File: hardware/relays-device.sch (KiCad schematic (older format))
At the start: 0 parts

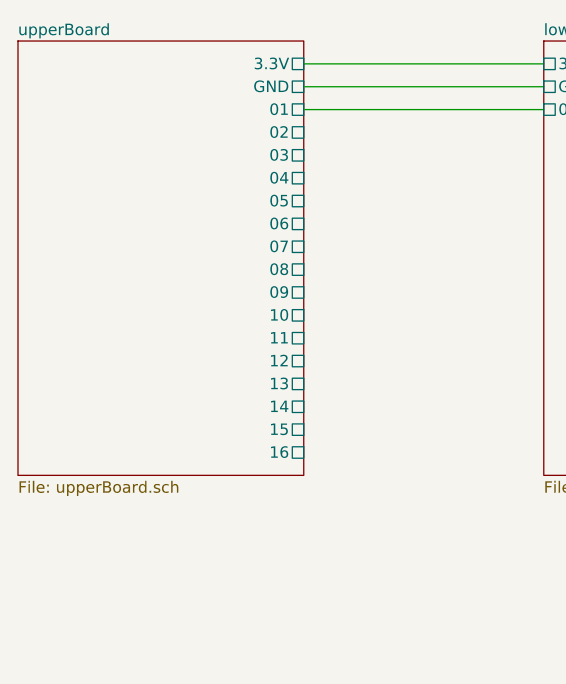
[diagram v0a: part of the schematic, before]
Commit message: replaced separated driver parts with driver chips and LED bars
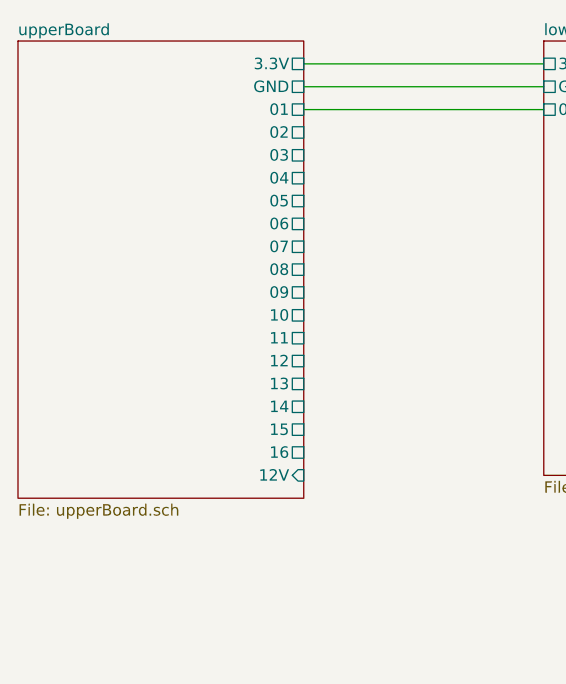
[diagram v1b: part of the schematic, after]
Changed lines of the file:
@@
 EESchema Schematic File Version 4
-LIBS:heating-control-cache
+LIBS:relays-device-cache
 EELAYER 30 0
 EELAYER END
 $Descr A4 11693 8268
 encoding utf-8
-Sheet 1 4
+Sheet 1 3
 Title ""
 Date ""
@@
 $EndDescr
 $Sheet
-S 1450 1450 1250 1900
+S 1450 1450 1250 2000
 U 5D9B8E7D
 F0 "upperBoard" 50
@@
 F18 "04" U R 2700 2050 50
 F19 "02" U R 2700 1850 50
+F20 "12V" I R 2700 3350 50
 $EndSheet
 $Sheet

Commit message: extracted relay to sub schematic to be able to multiply it
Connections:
- net labels removed: +12V, GND
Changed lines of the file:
@@
 $Descr A4 11693 8268
 encoding utf-8
-Sheet 1 3
+Sheet 1 5
 Title ""
 Date ""
@@
 F18 "04" U R 2700 2050 50
 F19 "02" U R 2700 1850 50
-F20 "12V" I R 2700 3350 50
+F20 "12V" U R 2700 3350 50
 $EndSheet
 $Sheet
-S 3750 1450 1250 1900
+S 3750 1450 1150 2000
 U 5D9FF064
 F0 "lowerBoard" 50
@@
 F3 "GND" U L 3750 1650 50
 F4 "01" U L 3750 1750 50
+F5 "12V" U L 3750 3350 50
+F6 "02" U L 3750 1850 50
 $EndSheet
 Wire Wire Line
@@
 Wire Wire Line
 	2700 1750 3750 1750
-$Comp
-L power:GND #PWR0102
-U 1 1 5DC08160
-P 3850 5200
-F 0 "#PWR0102" H 3850 4950 50  0001 C CNN
-F 1 "GND" H 3855 5027 50  0000 C CNN
-F 2 "" H 3850 5200 50  0001 C CNN
-F 3 "" H 3850 5200 50  0001 C CNN
-	1    3850 5200
-	1    0    0    -1
-$EndComp
-$Comp
-L power:PWR_FLAG #FLG0101
-U 1 1 5DC086BC
-P 3850 4900
-F 0 "#FLG0101" H 3850 4975 50  0001 C CNN
-F 1 "PWR_FLAG" H 3850 5073 50  0000 C CNN
-F 2 "" H 3850 4900 50  0001 C CNN
-F 3 "~" H 3850 4900 50  0001 C CNN
-	1    3850 4900
-	1    0    0    -1
-$EndComp
-$Comp
-L power:+12V #PWR0103
-U 1 1 5DC089A8
-P 3400 4900
-F 0 "#PWR0103" H 3400 4750 50  0001 C CNN
-F 1 "+12V" H 3415 5073 50  0000 C CNN
-F 2 "" H 3400 4900 50  0001 C CNN
-F 3 "" H 3400 4900 50  0001 C CNN
-	1    3400 4900
-	1    0    0    -1
-$EndComp
-$Comp
-L power:PWR_FLAG #FLG0102
-U 1 1 5DC08CFD
-P 3400 5200
-F 0 "#FLG0102" H 3400 5275 50  0001 C CNN
-F 1 "PWR_FLAG" H 3400 5373 50  0000 C CNN
-F 2 "" H 3400 5200 50  0001 C CNN
-F 3 "~" H 3400 5200 50  0001 C CNN
-	1    3400 5200
-	-1   0    0    1
-$EndComp
 Wire Wire Line
-	3850 5200 3850 4900
+	2700 3350 3750 3350
 Wire Wire Line
-	3400 5200 3400 4900
+	2700 1850 3750 1850
 $EndSCHEMATC

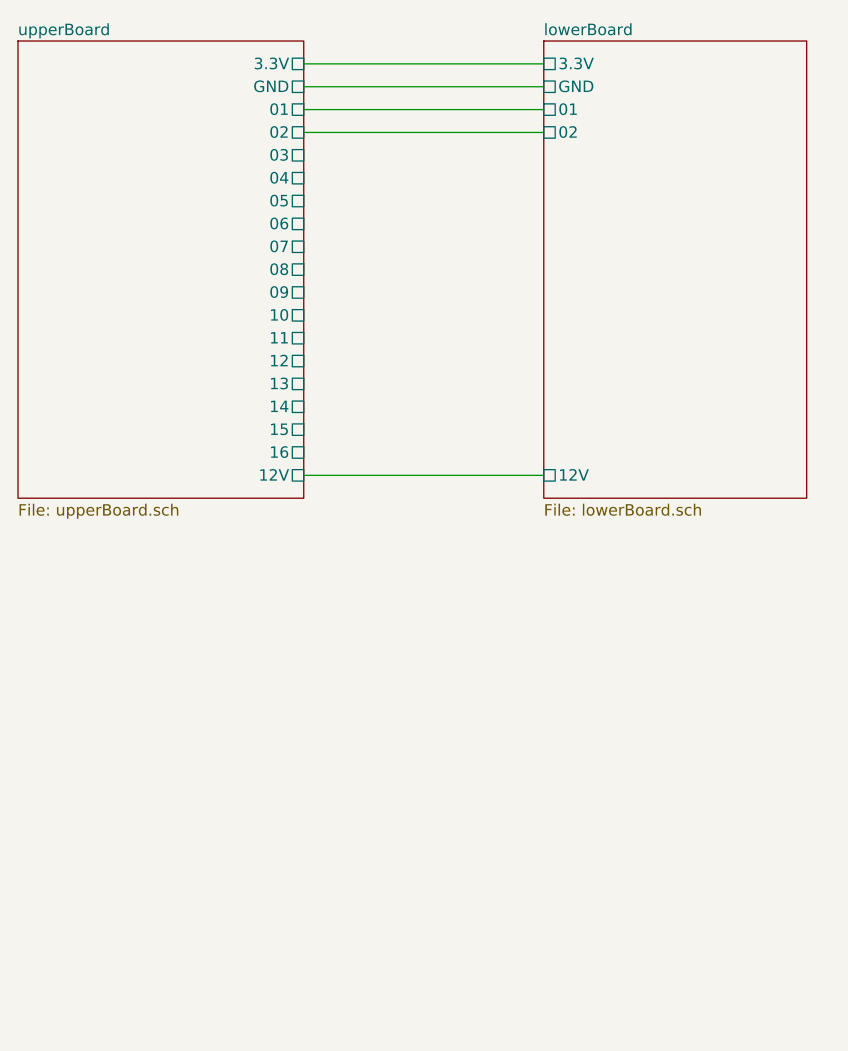
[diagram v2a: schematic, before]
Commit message: finished schematic mostly
started to create lower PCB
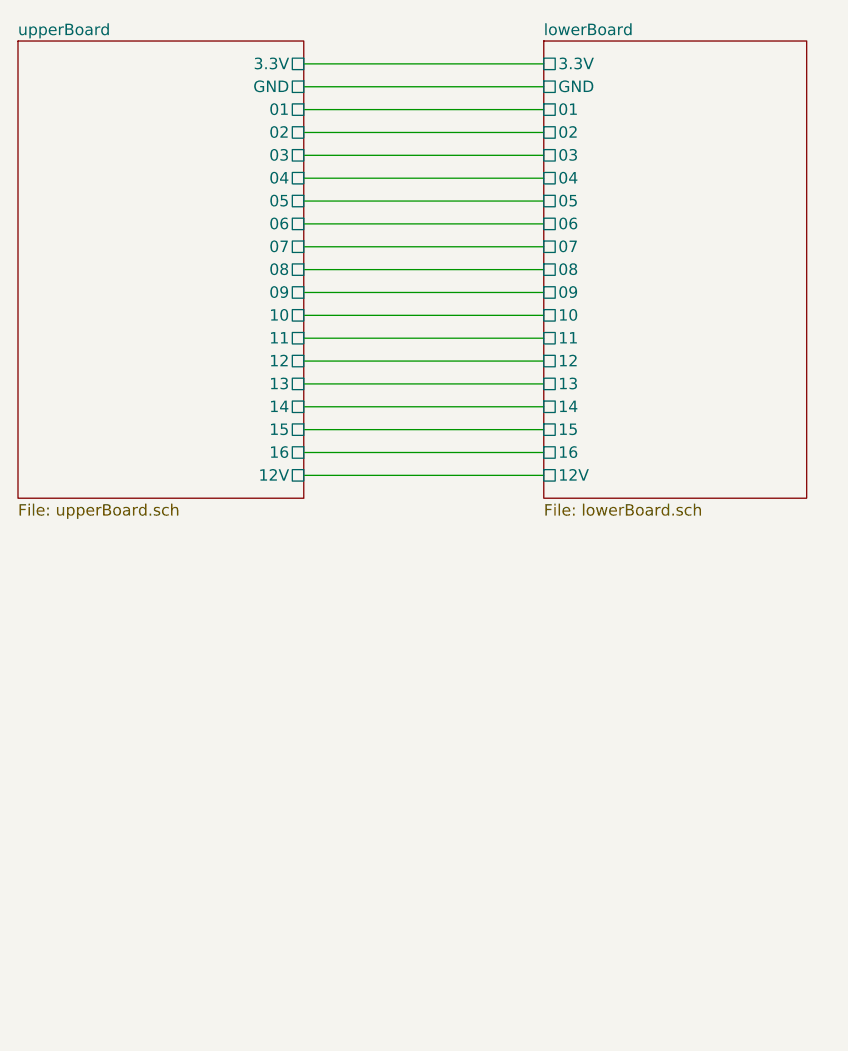
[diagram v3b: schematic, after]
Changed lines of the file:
@@
 $Descr A4 11693 8268
 encoding utf-8
-Sheet 1 5
+Sheet 1 19
 Title ""
 Date ""
@@
 F5 "12V" U L 3750 3350 50
 F6 "02" U L 3750 1850 50
+F7 "03" U L 3750 1950 50
+F8 "04" U L 3750 2050 50
+F9 "05" U L 3750 2150 50
+F10 "06" U L 3750 2250 50
+F11 "07" U L 3750 2350 50
+F12 "08" U L 3750 2450 50
+F13 "09" U L 3750 2550 50
+F14 "10" U L 3750 2650 50
+F15 "11" U L 3750 2750 50
+F16 "12" U L 3750 2850 50
+F17 "13" U L 3750 2950 50
+F18 "14" U L 3750 3050 50
+F19 "15" U L 3750 3150 50
+F20 "16" U L 3750 3250 50
 $EndSheet
 Wire Wire Line
@@
 Wire Wire Line
 	2700 1850 3750 1850
+Wire Wire Line
+	2700 1950 3750 1950
+Wire Wire Line
+	3750 2050 2700 2050
+Wire Wire Line
+	2700 2150 3750 2150
+Wire Wire Line
+	3750 2250 2700 2250
+Wire Wire Line
+	2700 2350 3750 2350
+Wire Wire Line
+	3750 2450 2700 2450
+Wire Wire Line
+	2700 2550 3750 2550
+Wire Wire Line
+	3750 2650 2700 2650
+Wire Wire Line
+	2700 2750 3750 2750
+Wire Wire Line
+	3750 2850 2700 2850
+Wire Wire Line
+	2700 2950 3750 2950
+Wire Wire Line
+	3750 3050 2700 3050
+Wire Wire Line
+	2700 3150 3750 3150
+Wire Wire Line
+	3750 3250 2700 3250
 $EndSCHEMATC
